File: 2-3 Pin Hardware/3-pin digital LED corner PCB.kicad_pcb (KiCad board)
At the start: 2 copper layers, 20.5 x 20.5 mm, 32 parts, among them J1 Conn_01x01_Male, J10 Conn_01x01_Male, J2 Conn_01x01_Male, J3 Conn_01x01_Male, J4 Conn_01x01_Male, J5 Conn_01x01_Male, J6 Conn_01x01_Male, J7 Conn_01x01_Male, J8 Conn_01x01_Male, J9 Conn_01x01_Male

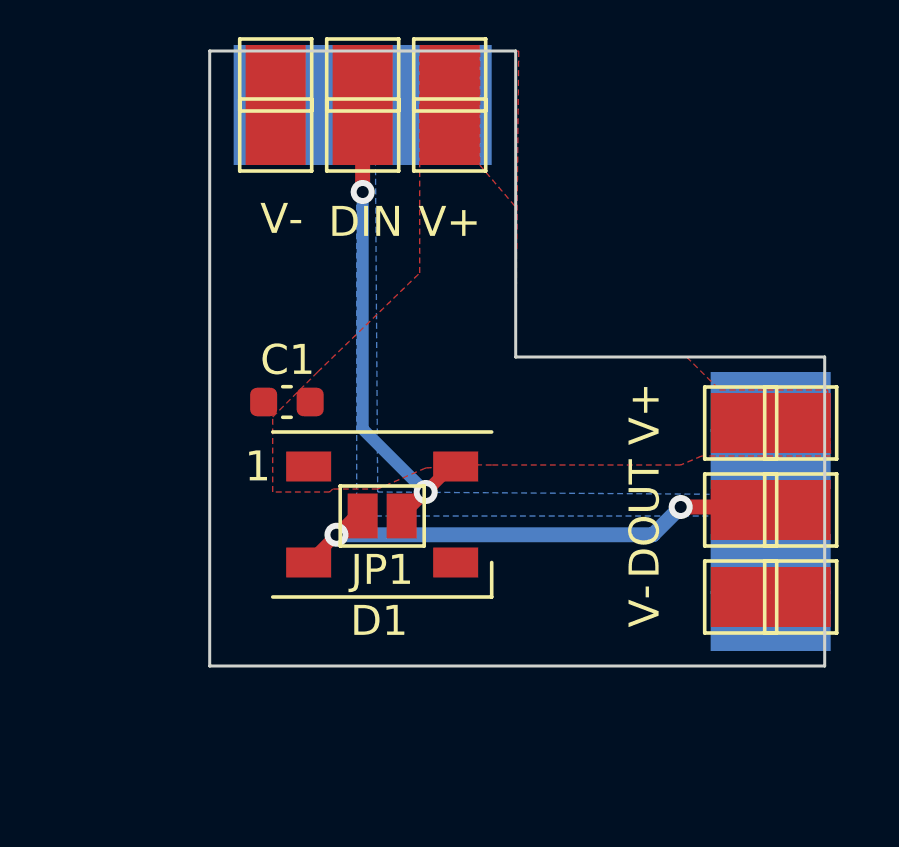
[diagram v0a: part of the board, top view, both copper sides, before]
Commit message: update 2-3 pin corner PCB
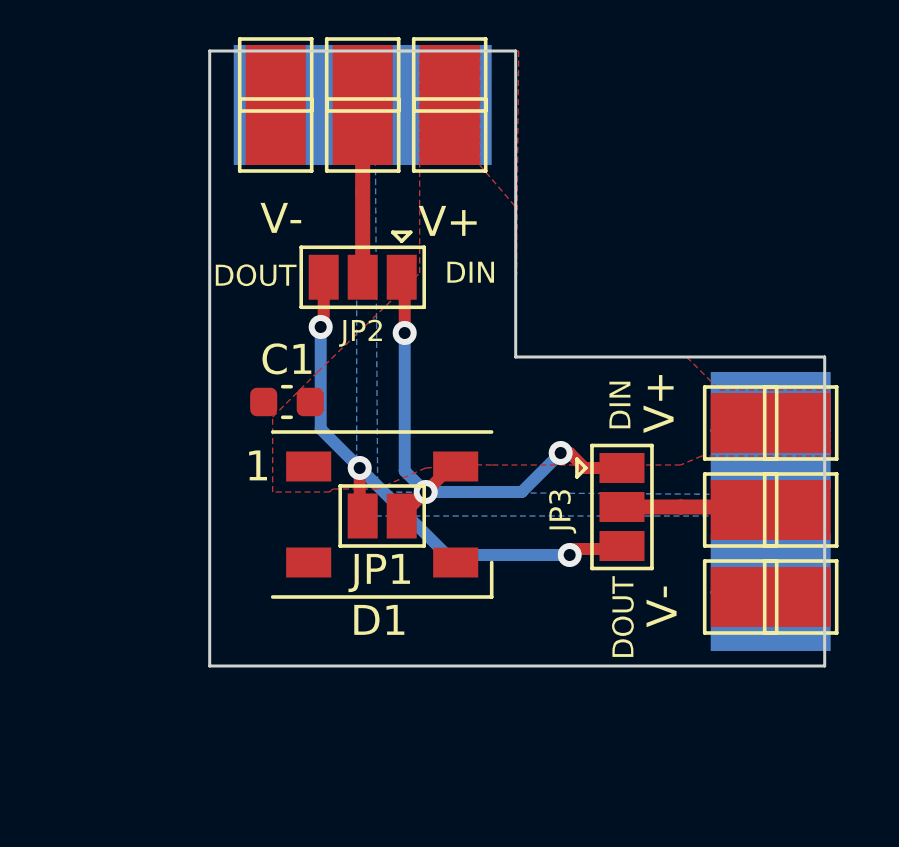
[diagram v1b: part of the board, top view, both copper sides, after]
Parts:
- added JP2: Jumper_3_Open, Jumper:SolderJumper-3_P1.3mm_Open_Pad1.0x1.5mm, F.Cu at (144.6, 112.0)
- added JP3: Jumper_3_Open, Jumper:SolderJumper-3_P1.3mm_Open_Pad1.0x1.5mm, F.Cu at (153.2, 119.7)
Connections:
- D1 pad 2: Net-(D1-Pad2) -> DOUT
- D1 pad 4: Net-(D1-Pad4) -> DIN
- J2 pad 1: Net-(D1-Pad4) -> K1 (x2)
- J5 pad 1: Net-(D1-Pad2) -> K2 (x2)
- JP1 pad 1: Net-(D1-Pad4) -> DIN
- JP1 pad 2: Net-(D1-Pad2) -> DOUT
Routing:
- net DOUT: track 0.00 -> 18.6 mm, vias 0 -> 3
- net DIN: track 0.00 -> 17.3 mm, vias 0 -> 3
- net Net-(D1-Pad2): track 16.5 -> 0.00 mm, vias 2 -> 0
- net Net-(D1-Pad4): track 15.0 -> 0.00 mm, vias 2 -> 0
- net K2: track 0.00 -> 4.16 mm
- net K1: track 0.00 -> 3.90 mm

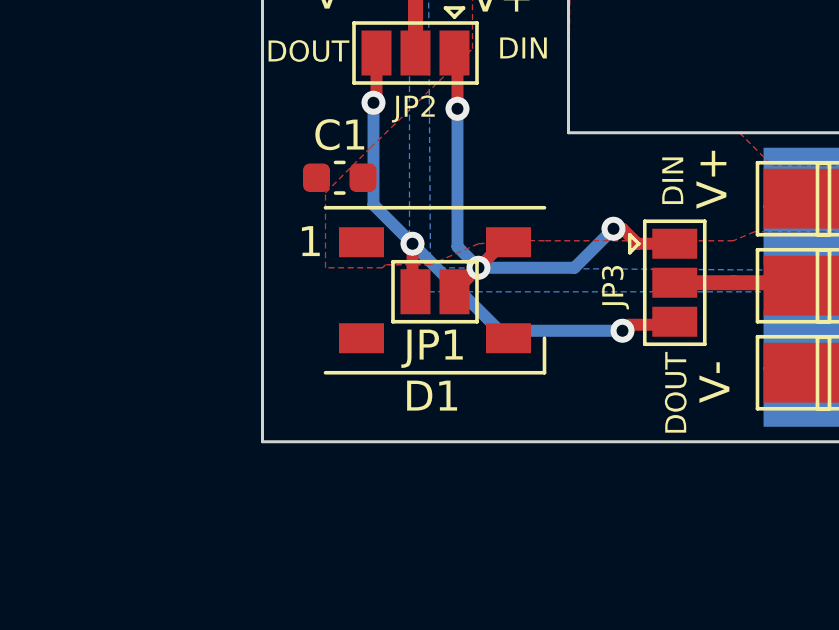
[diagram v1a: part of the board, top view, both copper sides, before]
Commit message: fix missing trace
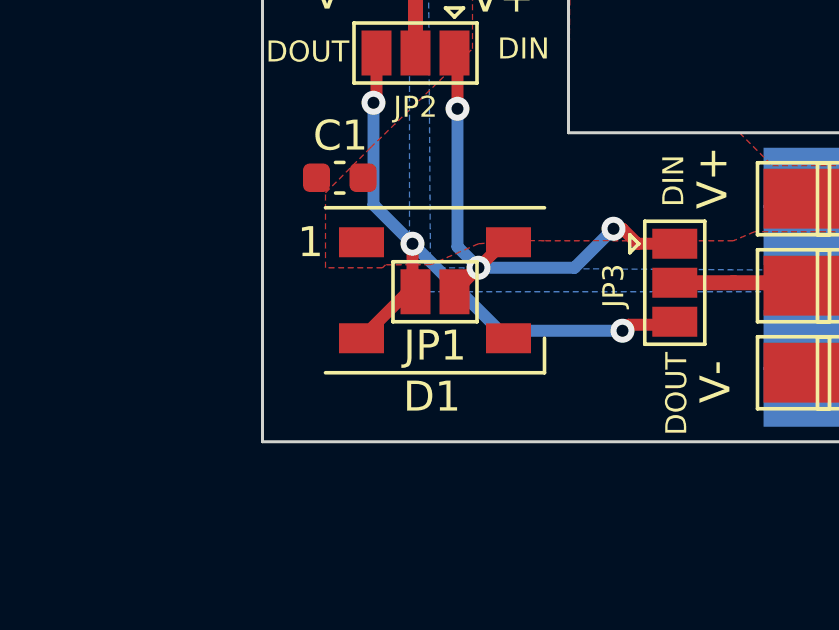
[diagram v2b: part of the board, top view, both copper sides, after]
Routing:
- net DOUT: track 18.6 -> 21.1 mm
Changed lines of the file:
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@@
   (segment (start 155.2 119.7) (end 153.2425 119.7) (width 0.5) (layer "F.Cu") (net 3))
   (segment (start 143.3 112.0425) (end 143.3 113.6) (width 0.4) (layer "F.Cu") (net 7))
+  (segment (start 144.6 120) (end 144.35 120) (width 0.4) (layer "F.Cu") (net 7))
   (segment (start 144.5 118.4) (end 144.5 119.9) (width 0.4) (layer "F.Cu") (net 7))
   (segment (start 153.1425 121.1) (end 153.2425 121) (width 0.4) (layer "F.Cu") (net 7))
+  (segment (start 144.35 120) (end 142.8 121.55) (width 0.4) (layer "F.Cu") (net 7))
   (segment (start 144.5 119.9) (end 144.6 120) (width 0.4) (layer "F.Cu") (net 7))
   (segment (start 151.7 121.1) (end 153.1425 121.1) (width 0.4) (layer "F.Cu") (net 7))
